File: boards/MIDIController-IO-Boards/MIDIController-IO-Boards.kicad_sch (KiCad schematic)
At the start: 41 parts, among them J1 KeyboardCtrl, J10 I2C, J11 I2CAddr, J12 IO_Boards, J13 I2C2, J14 DC12V, J2 TechnicsCtrl, J3 StopLeftCtrl, J4 StopRightCtrl, J5 TCA9548A 1, J6 PanelCtrl, J7 ToeStudCtrl, J8 TCA9548A 2, U1 LME78_05-1.0, U2 H11L1, U3 H11L1, U4 MAX3232

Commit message: Finished IO-Board PCB, switched RX/TX of board connectors for better routing
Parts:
- J1, J2, J3, J4, J6: footprint Connector_IDC:IDC-Header_2x05_P2.54mm_Vertical -> Connector_IDC:IDC-Header_2x05_P2.54mm_Horizontal
- R1, R2, R3: footprint Resistor_THT:R_Axial_DIN0204_L3.6mm_D1.6mm_P2.54mm_Vertical -> Resistor_THT:R_Axial_DIN0204_L3.6mm_D1.6mm_P7.62mm_Horizontal
- R4, R5, R6: footprint Resistor_THT:R_Axial_DIN0204_L3.6mm_D1.6mm_P2.54mm_Vertical -> Resistor_THT:R_Axial_DIN0207_L6.3mm_D2.5mm_P10.16mm_Horizontal
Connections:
- net +12V: now also J12.10 (Pin_10), J12.8 (Pin_8); no longer J12.2 (Pin_2), J12.4 (Pin_4)
- net +3.3V: now also J11.1 (Pin_1), J11.3 (Pin_3), J11.5 (Pin_5), J12.2 (Pin_2); no longer J12.14 (Pin_14)
- net +5V: now also J10.1 (Pin_1), J10.2 (Pin_2), J12.18 (Pin_18), J12.20 (Pin_20); no longer J10.5 (Pin_5), J10.6 (Pin_6), J11.1 (Pin_1), J11.3 (Pin_3), J11.5 (Pin_5), J12.6 (Pin_6), J12.8 (Pin_8)
- net GND: now also J12.12 (Pin_12), J12.14 (Pin_14); no longer J12.18 (Pin_18), J12.20 (Pin_20)
- net IntKeyboard: now also J12.11 (Pin_11); no longer J12.1 (Pin_1)
- net IntPanel: now also J12.1 (Pin_1); no longer J12.9 (Pin_9)
- net IntStopLeft: now also J12.3 (Pin_3); no longer J12.5 (Pin_5)
- net IntStopRight: now also J12.5 (Pin_5); no longer J12.7 (Pin_7)
- net IntTechnics: now also J12.9 (Pin_9); no longer J12.3 (Pin_3)
- net IntToeStud: now also J12.7 (Pin_7); no longer J12.11 (Pin_11)
- net MIDI_IN_Kbd: now also J1.3 (Pin_3); no longer J1.1 (Pin_1)
- net MIDI_IN_Technics: now also J2.3 (Pin_3); no longer J2.1 (Pin_1)
- net RS232_Panel_RXD: now also J6.3 (Pin_3); no longer J6.1 (Pin_1)
- net RS232_Panel_TXD: now also J6.1 (Pin_1); no longer J6.3 (Pin_3)
- net RXD_Kbd: now also J12.19 (Pin_19); no longer J12.17 (Pin_17)
- net RXD_Technics: now also J12.17 (Pin_17); no longer J12.19 (Pin_19)
- net SCL: now also J10.4 (Pin_4), J12.6 (Pin_6); no longer J10.1 (Pin_1), J12.12 (Pin_12)
- net SDA: now also J10.6 (Pin_6), J12.4 (Pin_4); no longer J10.3 (Pin_3), J12.10 (Pin_10)
- net SCL1 renamed SCL_Kbd
- net SCL_Kbd: now also J8.3 (Pin_3); no longer J5.10 (Pin_10)
- net SCL2 renamed SCL_I2C1
- net SCL_I2C1: now also J10.3 (Pin_3); no longer J2.7 (Pin_7)
- net SCL3 renamed SCL_StopLeft
- net SCL4 renamed SCL_StopRight
- net SCL5 renamed SCL_Panel
- net SCL_Panel: now also J5.9 (Pin_9); no longer J8.7 (Pin_7)
- net SCL6 renamed SCL_Technics
- net SCL_Technics: now also J2.7 (Pin_7); no longer J7.5
- removed net SCL7: J10.2 (Pin_2), J8.3 (Pin_3)
- net SCL8 renamed SCL_I2C2
- net SDA1 renamed SDA_Kbd
- net SDA_Kbd: now also J8.4 (Pin_4); no longer J5.9 (Pin_9)
- net SDA2 renamed SDA_I2C1
- net SDA_I2C1: now also J10.5 (Pin_5); no longer J2.9 (Pin_9)
- net SDA3 renamed SDA_StopLeft
- net SDA4 renamed SDA_StopRight
- net SDA5 renamed SDA_Panel
- net SDA_Panel: now also J5.10 (Pin_10); no longer J8.8 (Pin_8)
- net SDA6 renamed SDA_Technics
- net SDA_Technics: now also J2.9 (Pin_9); no longer J7.1
- removed net SDA7: J10.4 (Pin_4), J8.4 (Pin_4)
- net SDA8 renamed SDA_I2C2
- new net SCL_ToeStud: J7.5, J8.7 (Pin_7)
- new net SDA_ToeStud: J7.1, J8.8 (Pin_8)
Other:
- moved on the sheet: R1, R2, R3, R4

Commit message: Finished connectors on MIDIController board, fixed 3.3V IO voltage levels
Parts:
- C5, C6, C7, C8, C9: value 2.2µ -> 0.1uF
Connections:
- net +3.3V: now also C9.1, U4.16 (VCC)
- net +5V: no longer C9.1, U4.16 (VCC)
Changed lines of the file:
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@@
 			)
 		)
-		(property "Value" "2.2µ"
+		(property "Value" "0.1uF"
 			(at 173.101 92.583 0)
 			(effects
@@
 			)
 		)
-		(property "Value" "2.2µ"
+		(property "Value" "0.1uF"
 			(at 159.131 98.933 0)
 			(effects
@@
 			)
 		)
-		(property "Value" "2.2µ"
+		(property "Value" "0.1uF"
 			(at 165.608 112.776 0)
 			(effects
@@
 	)
 	(symbol
-		(lib_id "power:+5V")
-		(at 132.08 86.36 0)
-		(unit 1)
-		(exclude_from_sim no)
-		(in_bom yes)
-		(on_board yes)
-		(dnp no)
-		(fields_autoplaced yes)
-		(property "Reference" "#PWR050"
-			(at 132.08 90.17 0)
-			(effects
-				(font
-					(size 1.27 1.27)
-				)
-				(hide yes)
-			)
-		)
-		(property "Value" "+5V"
-			(at 132.08 81.28 0)
-			(effects
-				(font
-					(size 1.27 1.27)
-				)
-			)
-		)
-		(property "Footprint" ""
-			(at 132.08 86.36 0)
-			(effects
-				(font
-					(size 1.27 1.27)
-				)
-				(hide yes)
-			)
-		)
-		(property "Datasheet" ""
-			(at 132.08 86.36 0)
-			(effects
-				(font
-					(size 1.27 1.27)
-				)
-				(hide yes)
-			)
-		)
-		(property "Description" "Power symbol creates a global label with name \"+5V\""
-			(at 132.08 86.36 0)
-			(effects
-				(font
-					(size 1.27 1.27)
-				)
-				(hide yes)
-			)
-		)
-		(pin "1"
-		)
-		(instances
-			(project "MIDIController-IO-Boards"
-				(path "/06df47e9-b50a-4827-8ccb-76595e56d621"
-					(reference "#PWR050")
-					(unit 1)
-				)
-			)
-		)
-	)
-	(symbol
 		(lib_id "Mechanical:MountingHole")
 		(at 20.32 173.99 0)
@@
 	)
 	(symbol
-		(lib_id "power:+5V")
-		(at 170.18 87.63 0)
+		(lib_id "power:+3.3V")
+		(at 151.13 157.48 0)
 		(unit 1)
 		(exclude_from_sim no)
@@
 		(dnp no)
 		(fields_autoplaced yes)
-		(property "Reference" "#PWR054"
-			(at 170.18 91.44 0)
+		(property "Reference" "#PWR058"
+			(at 151.13 161.29 0)
 			(effects
 				(font
@@
 			)
 		)
-		(property "Value" "+5V"
-			(at 170.18 82.55 0)
+		(property "Value" "+3.3V"
+			(at 151.13 152.4 0)
 			(effects
 				(font
@@
 		)
 		(property "Footprint" ""
-			(at 170.18 87.63 0)
+			(at 151.13 157.48 0)
 			(effects
 				(font
@@
 		)
 		(property "Datasheet" ""
-			(at 170.18 87.63 0)
+			(at 151.13 157.48 0)
 			(effects
 				(font
@@
 			)
 		)
-		(property "Description" "Power symbol creates a global label with name \"+5V\""
-			(at 170.18 87.63 0)
+		(property "Description" "Power symbol creates a global label with name \"+3.3V\""
+			(at 151.13 157.48 0)
 			(effects
 				(font
@@
 			(project "MIDIController-IO-Boards"
 				(path "/06df47e9-b50a-4827-8ccb-76595e56d621"
-					(reference "#PWR054")
+					(reference "#PWR058")
 					(unit 1)
 				)
@@
 	(symbol
 		(lib_id "power:+3.3V")
-		(at 151.13 157.48 0)
+		(at 170.18 87.63 0)
 		(unit 1)
 		(exclude_from_sim no)
@@
 		(dnp no)
 		(fields_autoplaced yes)
-		(property "Reference" "#PWR058"
-			(at 151.13 161.29 0)
+		(property "Reference" "#PWR050"
+			(at 170.18 91.44 0)
 			(effects
 				(font
@@
 		)
 		(property "Value" "+3.3V"
-			(at 151.13 152.4 0)
+			(at 170.18 82.55 0)
 			(effects
 				(font
@@
 		)
 		(property "Footprint" ""
-			(at 151.13 157.48 0)
+			(at 170.18 87.63 0)
 			(effects
 				(font
@@
 		)
 		(property "Datasheet" ""
-			(at 151.13 157.48 0)
+			(at 170.18 87.63 0)
 			(effects
 				(font
@@
 		)
 		(property "Description" "Power symbol creates a global label with name \"+3.3V\""
-			(at 151.13 157.48 0)
+			(at 170.18 87.63 0)
 			(effects
 				(font
@@
 			(project "MIDIController-IO-Boards"
 				(path "/06df47e9-b50a-4827-8ccb-76595e56d621"
-					(reference "#PWR058")
+					(reference "#PWR050")
 					(unit 1)
 				)
@@
 			)
 		)
-		(property "Value" "2.2µ"
+		(property "Value" "0.1uF"
 			(at 165.862 104.648 0)
 			(effects
@@
 	)
 	(symbol
+		(lib_id "power:+3.3V")
+		(at 132.08 86.36 0)
+		(unit 1)
+		(exclude_from_sim no)
+		(in_bom yes)
+		(on_board yes)
+		(dnp no)
+		(fields_autoplaced yes)
+		(property "Reference" "#PWR054"
+			(at 132.08 90.17 0)
+			(effects
+				(font
+					(size 1.27 1.27)
+				)
+				(hide yes)
+			)
+		)
+		(property "Value" "+3.3V"
+			(at 132.08 81.28 0)
+			(effects
+				(font
+					(size 1.27 1.27)
+				)
+			)
+		)
+		(property "Footprint" ""
+			(at 132.08 86.36 0)
+			(effects
+				(font
+					(size 1.27 1.27)
+				)
+				(hide yes)
+			)
+		)
+		(property "Datasheet" ""
+			(at 132.08 86.36 0)
+			(effects
+				(font
+					(size 1.27 1.27)
+				)
+				(hide yes)
+			)
+		)
+		(property "Description" "Power symbol creates a global label with name \"+3.3V\""
+			(at 132.08 86.36 0)
+			(effects
+				(font
+					(size 1.27 1.27)
+				)
+				(hide yes)
+			)
+		)
+		(pin "1"
+		)
+		(instances
+			(project "MIDIController-IO-Boards"
+				(path "/06df47e9-b50a-4827-8ccb-76595e56d621"
+					(reference "#PWR054")
+					(unit 1)
+				)
+			)
+		)
+	)
+	(symbol
 		(lib_id "power:PWR_FLAG")
 		(at 207.01 149.86 270)
@@
 			)
 		)
-		(property "Value" "2.2µ"
+		(property "Value" "0.1uF"
 			(at 110.871 98.933 0)
 			(effects

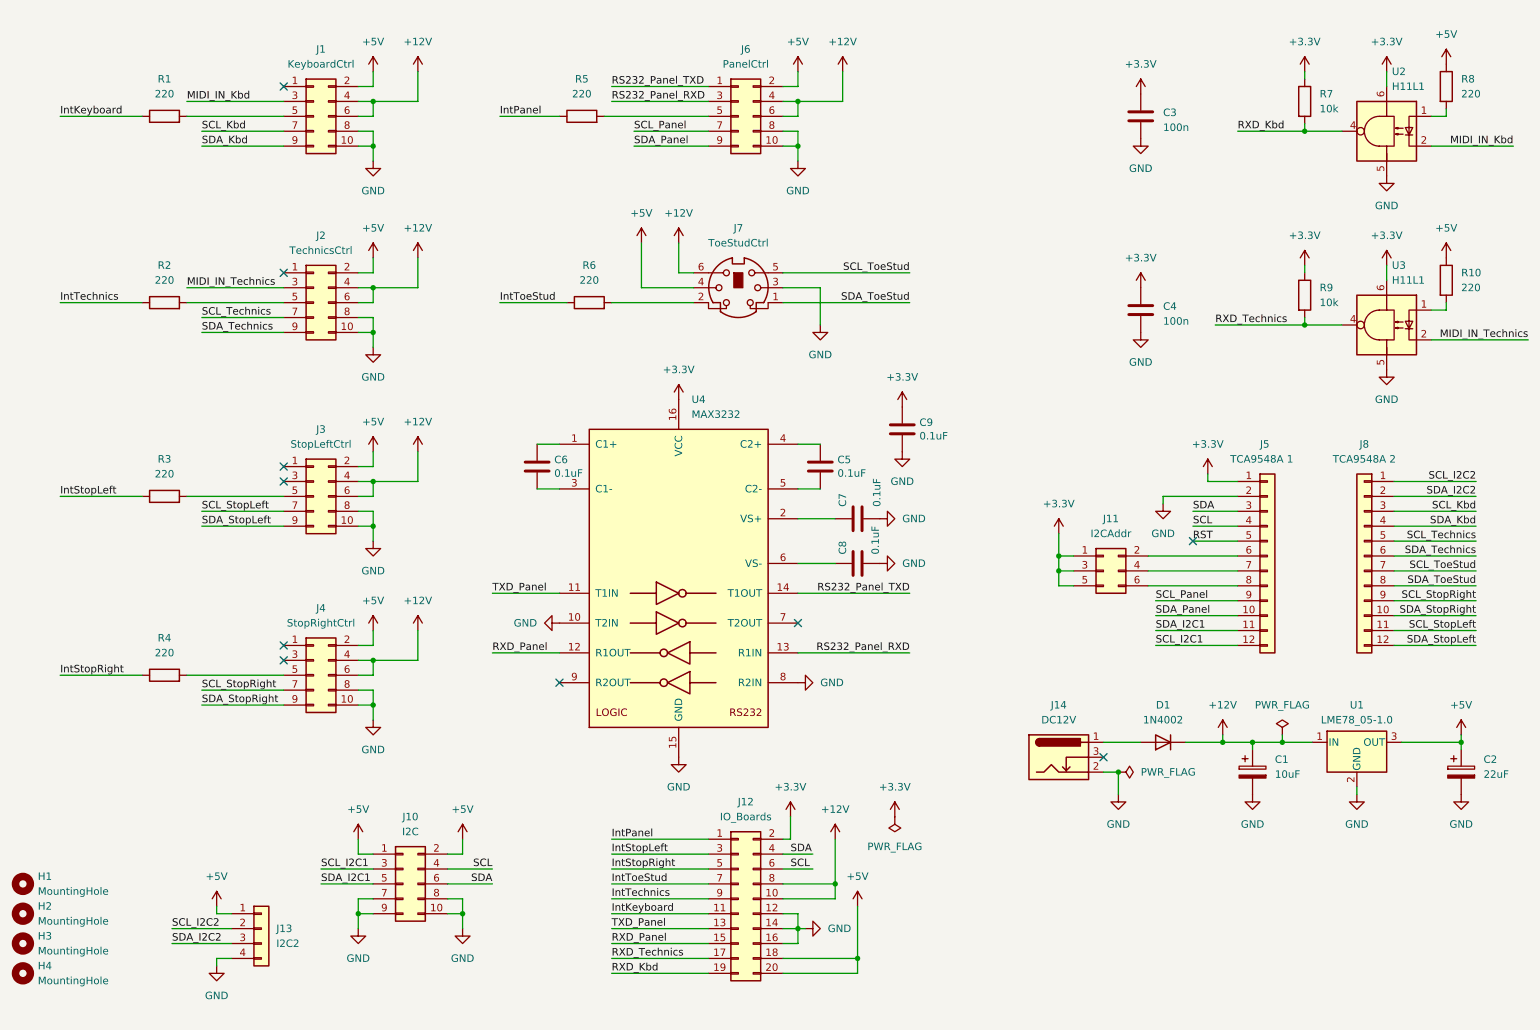
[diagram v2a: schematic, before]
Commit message: Fixed interrupt line to use open collector, added pullups to I2C lines
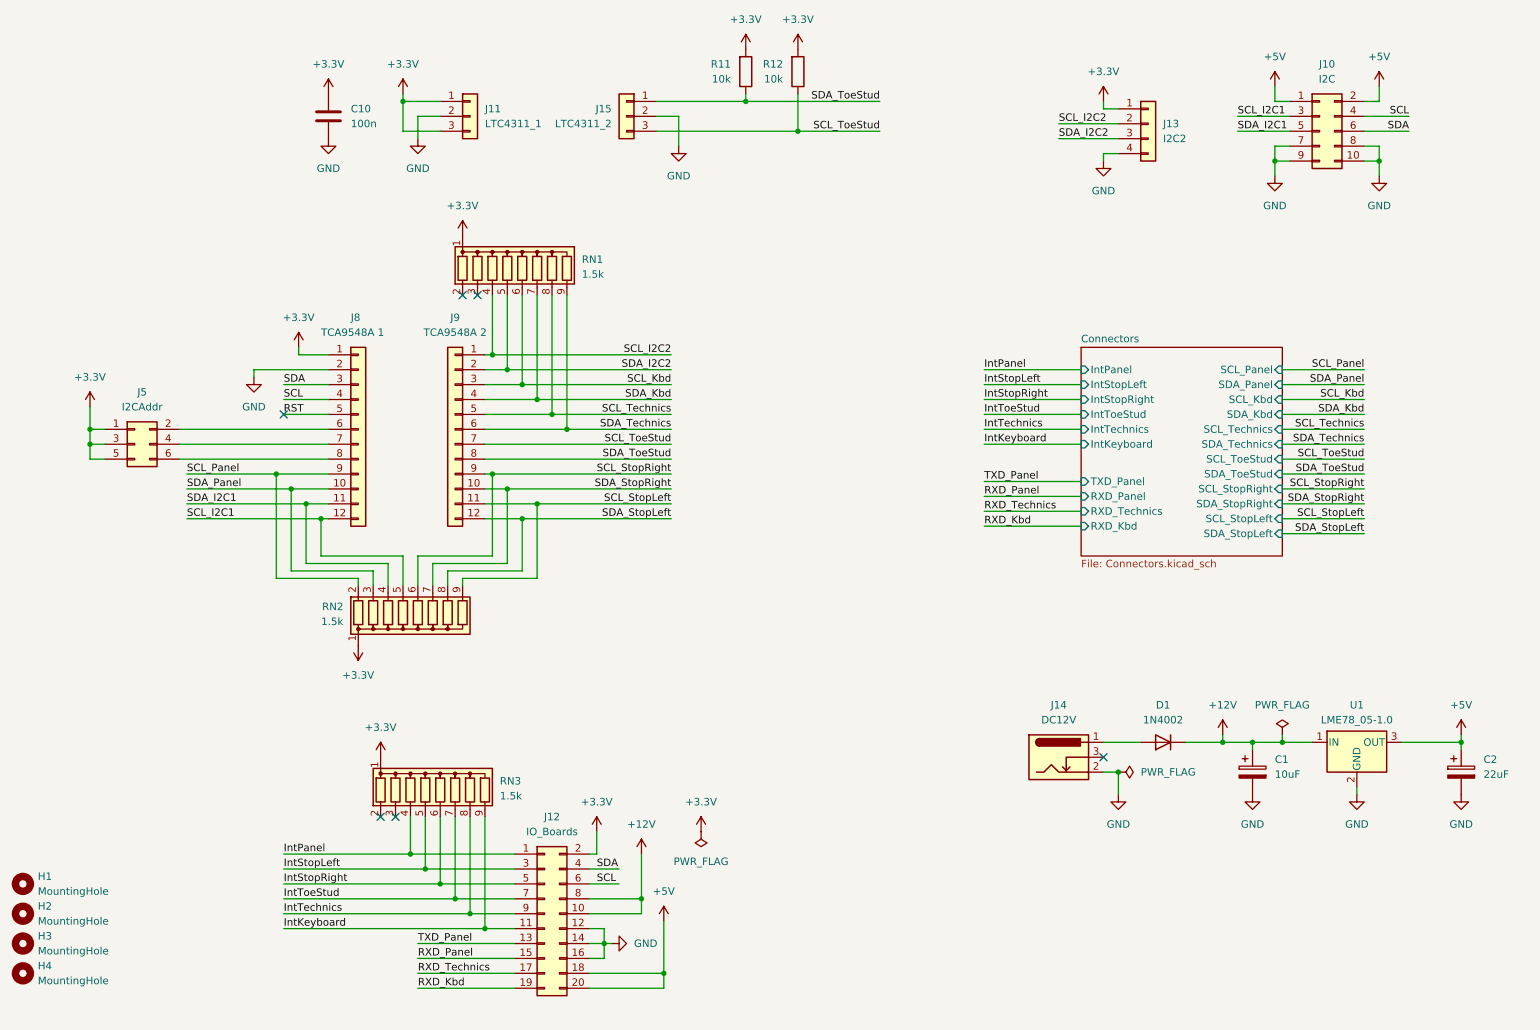
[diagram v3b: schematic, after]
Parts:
- removed C3, C4: 100n, Capacitor_THT:C_Disc_D5.0mm_W2.5mm_P5.00mm, symbol Device:C
- removed C5, C6, C7, C8, C9: 0.1uF, Capacitor_THT:C_Rect_L4.6mm_W3.0mm_P2.50mm_MKS02_FKP02, symbol Device:C
- removed J1: KeyboardCtrl, Connector_IDC:IDC-Header_2x05_P2.54mm_Horizontal, symbol Connector_Generic:Conn_02x05_Odd_Even
- removed J11: I2CAddr, Connector_PinHeader_2.54mm:PinHeader_2x03_P2.54mm_Vertical, symbol Connector_Generic:Conn_02x03_Odd_Even
- removed J2: TechnicsCtrl, Connector_IDC:IDC-Header_2x05_P2.54mm_Horizontal, symbol Connector_Generic:Conn_02x05_Odd_Even
- removed J3: StopLeftCtrl, Connector_IDC:IDC-Header_2x05_P2.54mm_Horizontal, symbol Connector_Generic:Conn_02x05_Odd_Even
- removed J4: StopRightCtrl, Connector_IDC:IDC-Header_2x05_P2.54mm_Horizontal, symbol Connector_Generic:Conn_02x05_Odd_Even
- removed J5: TCA9548A 1, Connector_PinSocket_2.54mm:PinSocket_1x12_P2.54mm_Vertical, symbol Connector_Generic:Conn_01x12
- removed J6: PanelCtrl, Connector_IDC:IDC-Header_2x05_P2.54mm_Horizontal, symbol Connector_Generic:Conn_02x05_Odd_Even
- removed J7: ToeStudCtrl, SnapEDA:MiniDIN TE_5749180-1, symbol Connector:Mini-DIN-6
- removed R1, R10, R2, R3, R8: 220, Resistor_THT:R_Axial_DIN0204_L3.6mm_D1.6mm_P7.62mm_Horizontal, symbol Device:R
- removed R4, R5, R6: 220, Resistor_THT:R_Axial_DIN0207_L6.3mm_D2.5mm_P10.16mm_Horizontal, symbol Device:R
- removed R7, R9: 10k, Resistor_THT:R_Axial_DIN0204_L3.6mm_D1.6mm_P7.62mm_Horizontal, symbol Device:R
- removed U2, U3: H11L1, Package_DIP:DIP-6_W7.62mm, symbol Isolator:H11L1
- removed U4: MAX3232, Package_DIP:DIP-16_W7.62mm, symbol Interface_UART:MAX3232
- added C10: 100n, Capacitor_THT:C_Disc_D5.0mm_W2.5mm_P5.00mm, symbol Device:C
- added J11: LTC4311_1, Connector_PinSocket_2.54mm:PinSocket_1x03_P2.54mm_Vertical, symbol Connector_Generic:Conn_01x03
- added J15: LTC4311_2, Connector_PinSocket_2.54mm:PinSocket_1x03_P2.54mm_Vertical, symbol Connector_Generic:Conn_01x03
- added J5: I2CAddr, Connector_PinHeader_2.54mm:PinHeader_2x03_P2.54mm_Vertical, symbol Connector_Generic:Conn_02x03_Odd_Even
- added J9: TCA9548A 2, Connector_PinSocket_2.54mm:PinSocket_1x12_P2.54mm_Vertical, symbol Connector_Generic:Conn_01x12
- added R11, R12: 10k, Resistor_THT:R_Axial_DIN0207_L6.3mm_D2.5mm_P10.16mm_Horizontal, symbol Device:R
- added RN1, RN2, RN3: 1.5k, Resistor_THT:R_Array_SIP9, symbol Device:R_Network08
- J8: value TCA9548A 2 -> TCA9548A 1
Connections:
- net +3.3V: now also J13.1 (Pin_1), J8.1 (Pin_1), C10.1, J11.1 (Pin_1), J11.3 (Pin_3), J5.1 (Pin_1), J5.3 (Pin_3), J5.5 (Pin_5), R11.2, R12.2, RN1.1 (common), RN2.1 (common), RN3.1 (common)
- net +5V: no longer J13.1 (Pin_1)
- net GND: now also J8.2 (Pin_2), C10.2, J11.2 (Pin_2), J15.2 (Pin_2)
- net IntKeyboard: now also RN3.9 (R8)
- net IntPanel: now also RN3.4 (R3)
- net IntStopLeft: now also RN3.5 (R4)
- net IntStopRight: now also RN3.6 (R5)
- net IntTechnics: now also RN3.8 (R7)
- net IntToeStud: now also RN3.7 (R6)
- net RST: now also J8.5 (Pin_5)
- net SCL: now also J8.4 (Pin_4)
- net SCL_I2C1: now also J8.12 (Pin_12), RN2.5 (R4)
- net SCL_I2C2: now also J9.1 (Pin_1), RN1.4 (R3); no longer J8.1 (Pin_1)
- net SCL_Kbd: now also J9.3 (Pin_3), RN1.6 (R5); no longer J8.3 (Pin_3)
- net SCL_Panel: now also J8.9 (Pin_9), RN2.2 (R1)
- net SCL_StopLeft: now also J9.11 (Pin_11), RN2.9 (R8); no longer J8.11 (Pin_11)
- net SCL_StopRight: now also J9.9 (Pin_9), RN2.6 (R5); no longer J8.9 (Pin_9)
- net SCL_Technics: now also J9.5 (Pin_5), RN1.8 (R7); no longer J8.5 (Pin_5)
- net SCL_ToeStud: now also J15.3 (Pin_3), J9.7 (Pin_7), R12.1; no longer J8.7 (Pin_7)
- net SDA: now also J8.3 (Pin_3)
- net SDA_I2C1: now also J8.11 (Pin_11), RN2.4 (R3)
- net SDA_I2C2: now also J9.2 (Pin_2), RN1.5 (R4); no longer J8.2 (Pin_2)
- net SDA_Kbd: now also J9.4 (Pin_4), RN1.7 (R6); no longer J8.4 (Pin_4)
- net SDA_Panel: now also J8.10 (Pin_10), RN2.3 (R2)
- net SDA_StopLeft: now also J9.12 (Pin_12), RN2.8 (R7); no longer J8.12 (Pin_12)
- net SDA_StopRight: now also J9.10 (Pin_10), RN2.7 (R6); no longer J8.10 (Pin_10)
- net SDA_Technics: now also J9.6 (Pin_6), RN1.9 (R8); no longer J8.6 (Pin_6)
- net SDA_ToeStud: now also J15.1 (Pin_1), J9.8 (Pin_8), R11.1; no longer J8.8 (Pin_8)
- new net: J5.2 (Pin_2), J8.6 (Pin_6)
- new net: J5.4 (Pin_4), J8.7 (Pin_7)
- new net: J5.6 (Pin_6), J8.8 (Pin_8)
- no-connect marks 10 -> 6
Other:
- added sheet Connectors (Connectors.kicad_sch)
- moved on the sheet: J10, J12, J13

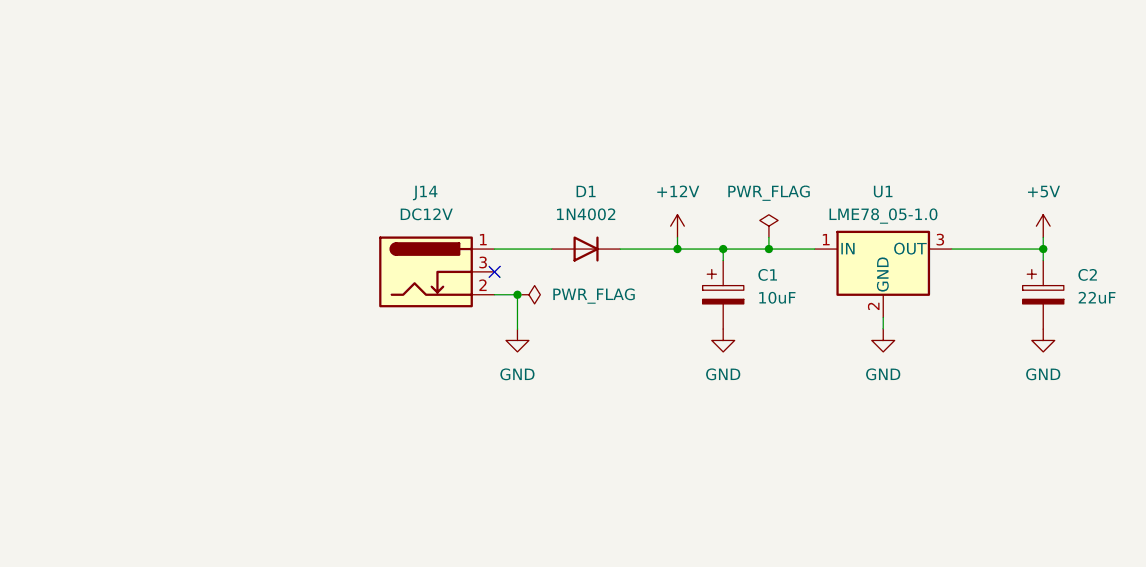
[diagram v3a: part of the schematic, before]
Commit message: Added bypass caps to power supplies, use cheaper MAX232 IC.
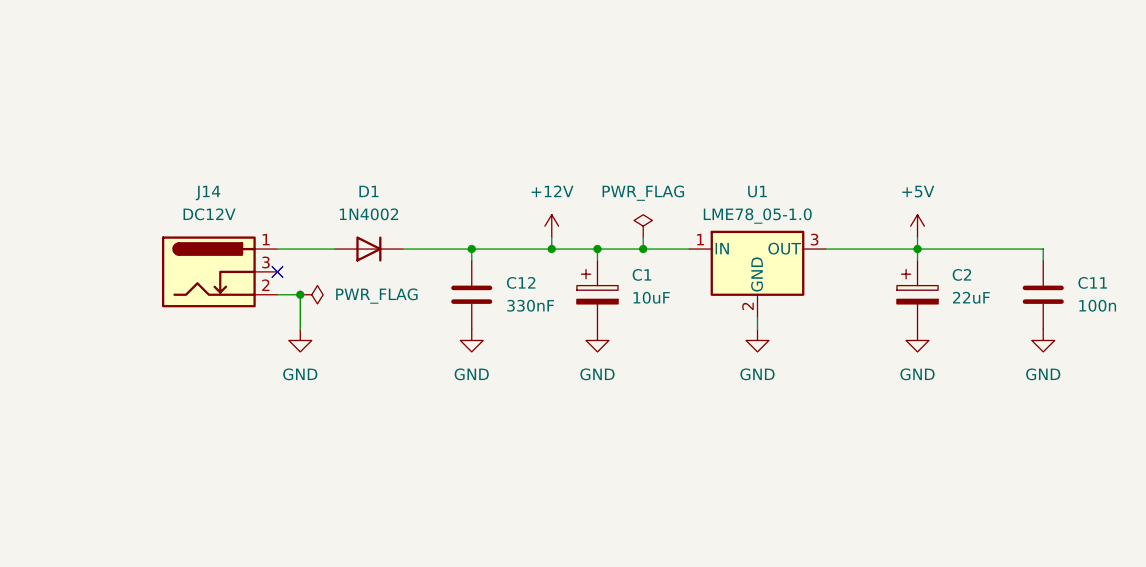
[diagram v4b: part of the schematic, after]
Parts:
- added C11: 100n, Capacitor_THT:C_Disc_D5.0mm_W2.5mm_P5.00mm, symbol Device:C
- added C12: 330nF, Capacitor_THT:C_Disc_D5.0mm_W2.5mm_P5.00mm, symbol Device:C
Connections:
- net +12V: now also C12.1
- net +5V: now also C11.1
- net GND: now also C11.2, C12.2
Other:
- moved on the sheet: C1, C2, D1, J14, U1

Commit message: Updated design rules to 0.32mm template and exported Gerber files
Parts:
- C1: footprint Capacitor_THT:CP_Radial_D6.3mm_P2.50mm -> Capacitor_THT:CP_Radial_D5.0mm_P2.00mm
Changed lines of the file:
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@@
 			)
 		)
-		(property "Footprint" "Capacitor_THT:CP_Radial_D6.3mm_P2.50mm"
+		(property "Footprint" "Capacitor_THT:CP_Radial_D5.0mm_P2.00mm"
 			(at 216.8652 153.67 0)
 			(effects
